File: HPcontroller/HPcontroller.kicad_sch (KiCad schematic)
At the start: 8 parts, among them J5 54-00174, U7 Adafruit_QTPY_ESP32-C3

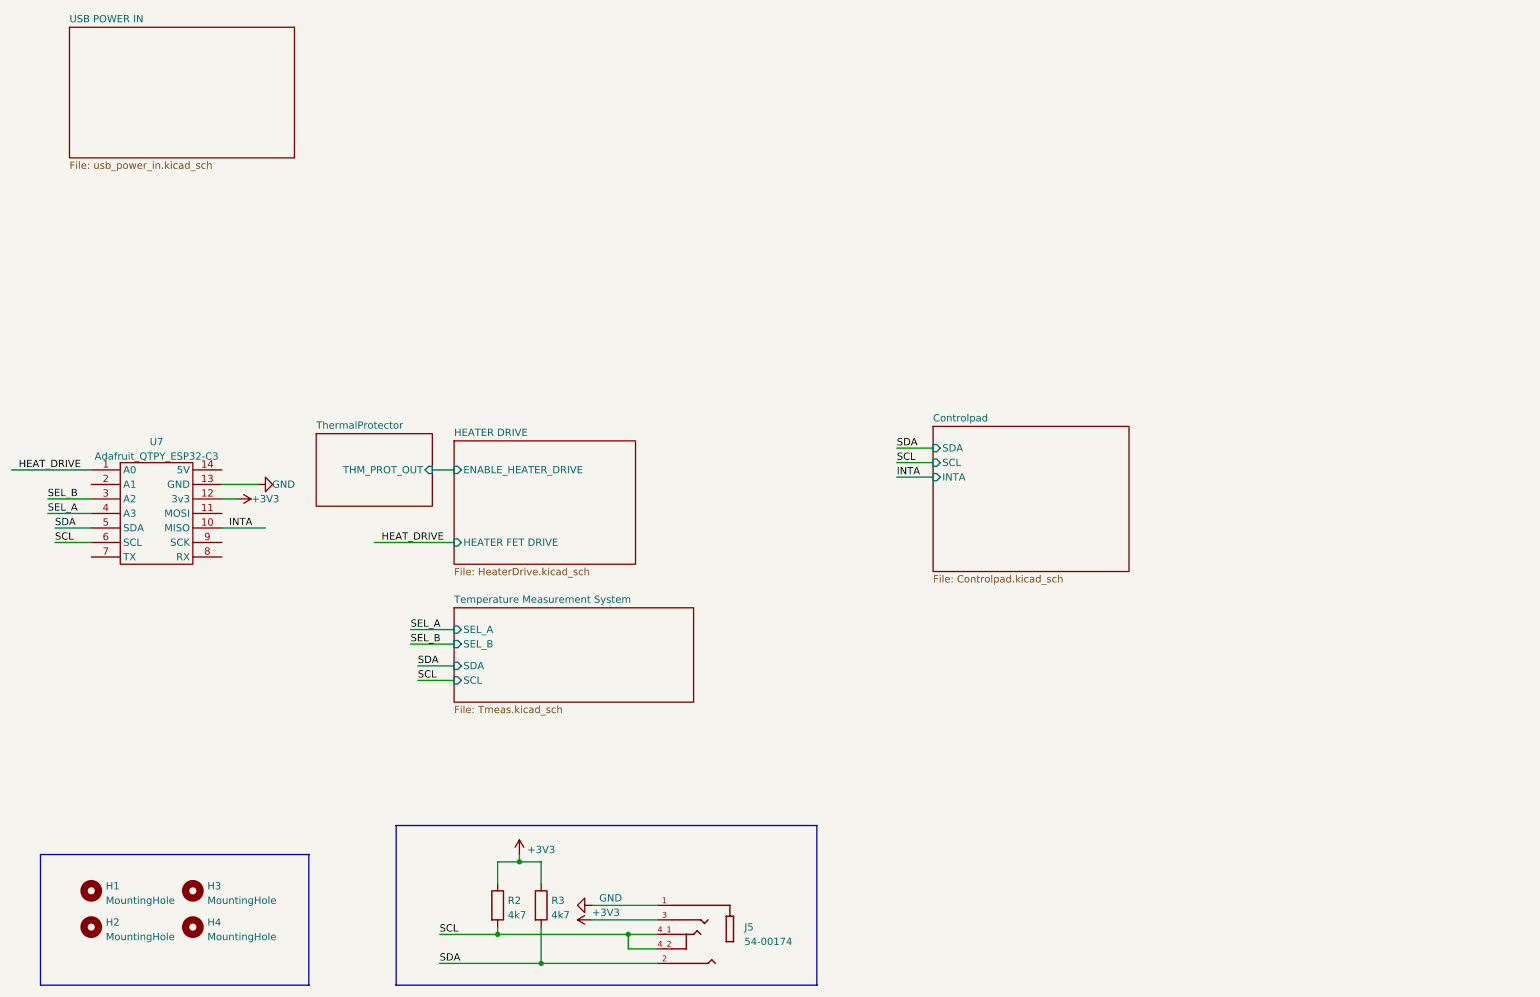
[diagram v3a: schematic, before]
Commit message: worked on bom, orderables from dk are in
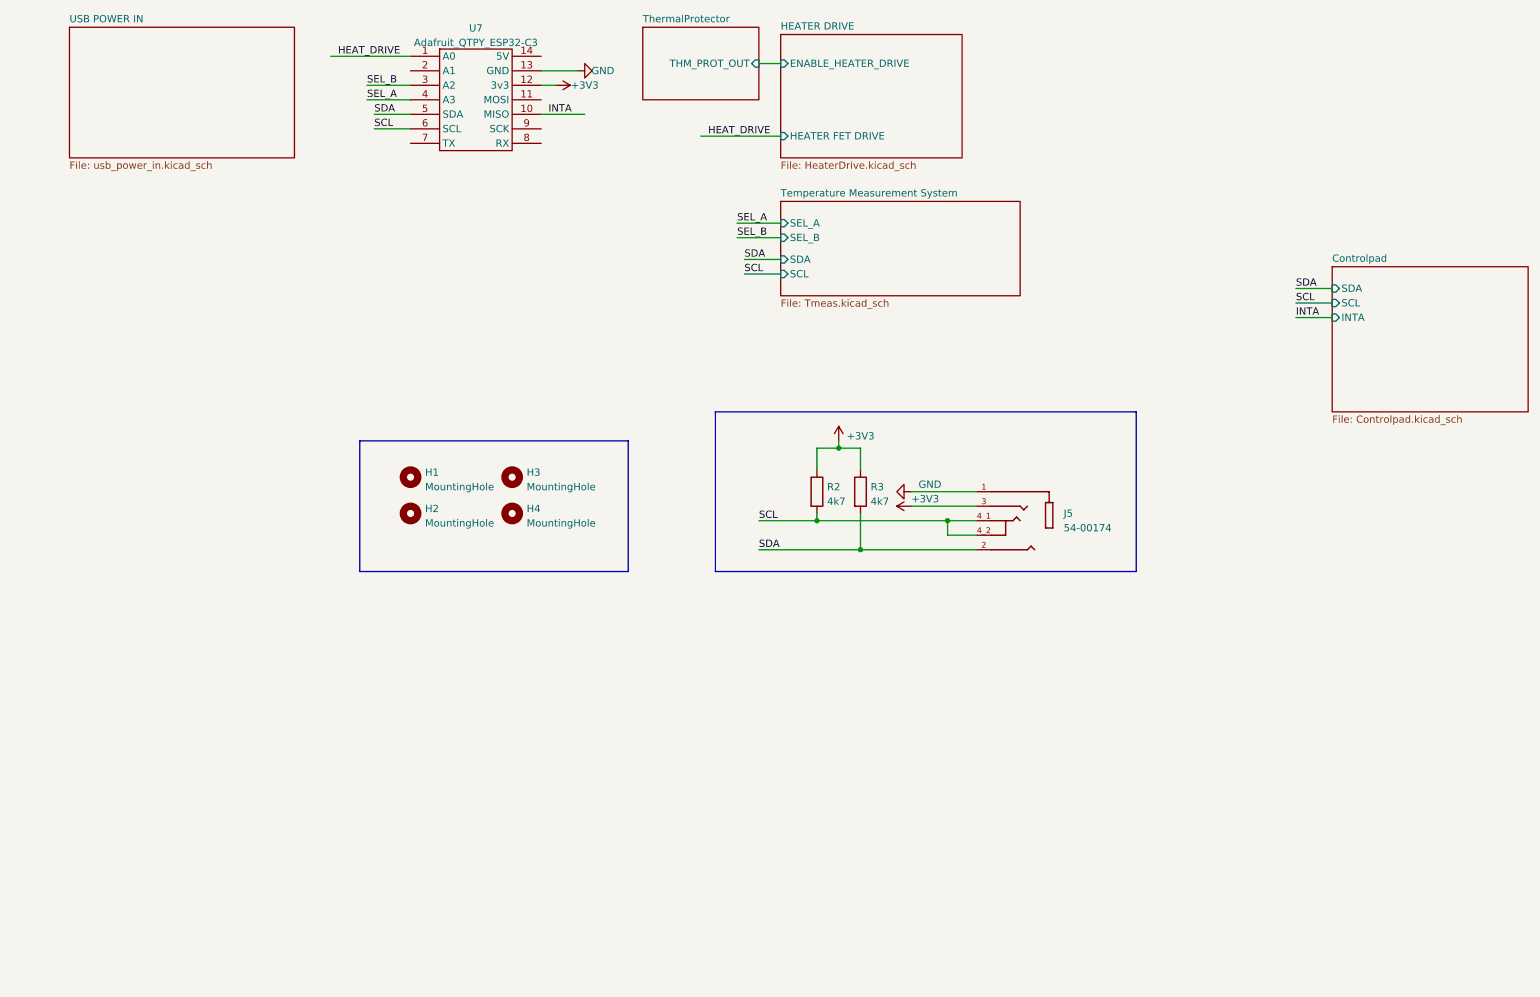
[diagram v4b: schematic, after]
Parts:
- J5: Digikey PN (none) -> 839-54-00174CT-ND; SNAPEDA_PN 54-00174 -> (none)
- R2, R3: Digikey PN (none) -> 311-4.7KARCT-ND; MPN (none) -> RC0805JR-074K7L
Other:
- moved on the sheet: H1, H2, H3, H4, J5, R2, R3, U7

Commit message: v3 routing
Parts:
- U7: footprint HPfootprint:QTPY ESP32 C3 -> hotplate_Library:XIAO-ESP32C3-SMD-cutout
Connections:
- net INTA: no longer names the net of U7.10 (MISO)
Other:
- removed sheet Controlpad

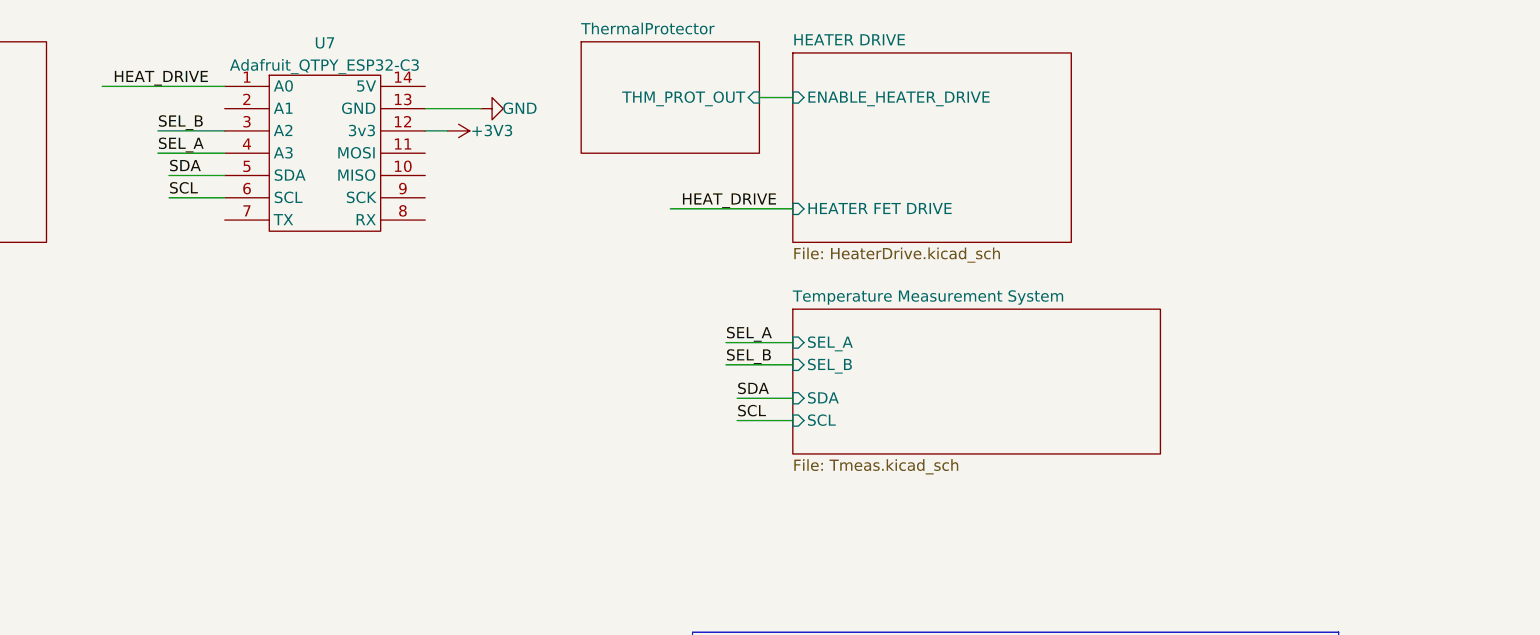
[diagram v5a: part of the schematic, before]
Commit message: new temp circuit
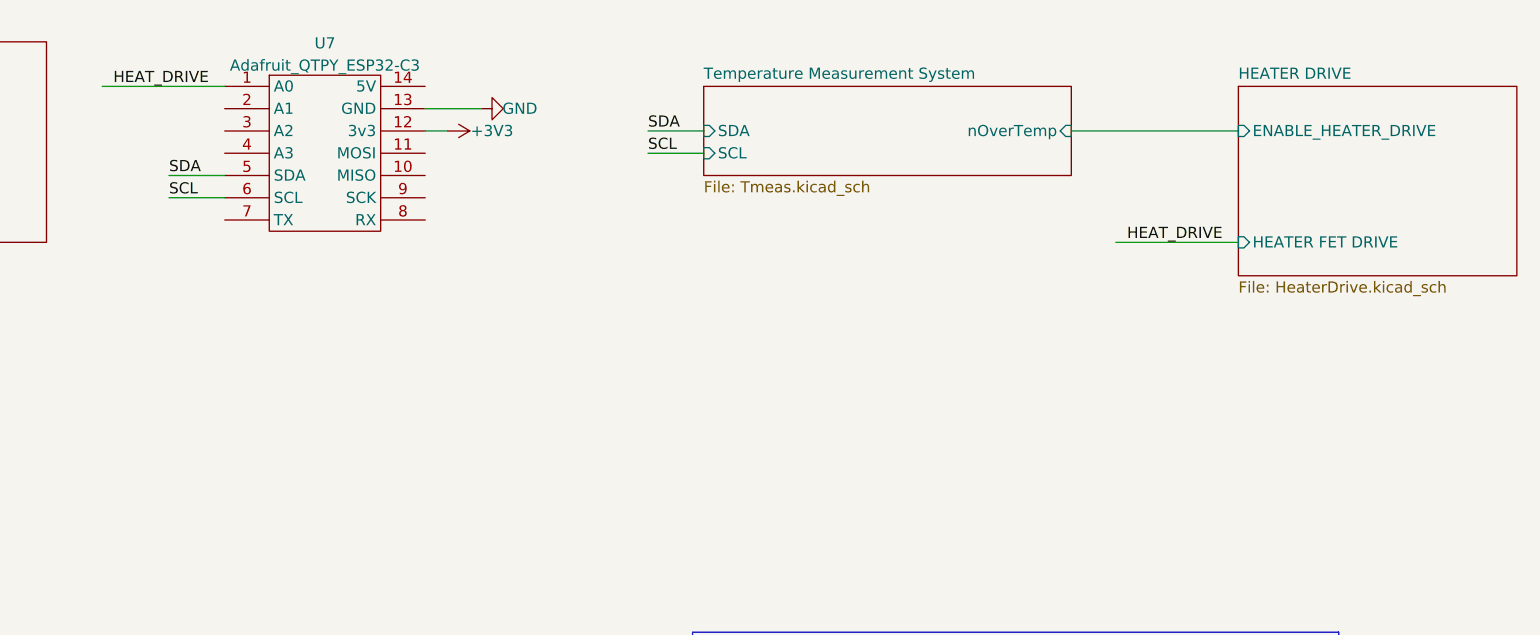
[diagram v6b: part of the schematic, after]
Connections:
- net SEL_A: no longer names the net of U7.4 (A3)
- net SEL_B: no longer names the net of U7.3 (A2)
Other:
- removed sheet ThermalProtector
- sheet Temperature Measurement System ports: added nOverTemp; removed SEL_A, SEL_B
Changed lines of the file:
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@@
 	(wire
 		(pts
-			(xy 144.78 66.04) (xy 151.13 66.04)
+			(xy 134.62 35.56) (xy 140.97 35.56)
 		)
 		(stroke
@@
 	(wire
 		(pts
-			(xy 78.74 35.56) (xy 86.36 35.56)
-		)
-		(stroke
-			(width 0)
-			(type default)
-		)
-	)
-	(wire
-		(pts
-			(xy 143.51 62.23) (xy 151.13 62.23)
-		)
-		(stroke
-			(width 0)
-			(type default)
-		)
-	)
-	(wire
-		(pts
 			(xy 180.34 114.3) (xy 180.34 111.76)
 		)
@@
 	(wire
 		(pts
-			(xy 144.78 68.58) (xy 151.13 68.58)
+			(xy 134.62 38.1) (xy 140.97 38.1)
 		)
 		(stroke
@@
 	(wire
 		(pts
+			(xy 182.88 35.56) (xy 201.93 35.56)
+		)
+		(stroke
+			(width 0)
+			(type default)
+		)
+	)
+	(wire
+		(pts
 			(xy 161.29 99.06) (xy 165.1 99.06)
 		)
@@
 	(wire
 		(pts
-			(xy 147.32 31.75) (xy 151.13 31.75)
-		)
-		(stroke
-			(width 0)
-			(type default)
-		)
-	)
-	(wire
-		(pts
 			(xy 165.1 116.84) (xy 185.42 116.84)
 		)
@@
 	(wire
 		(pts
-			(xy 137.16 44.45) (xy 151.13 44.45)
+			(xy 187.96 48.26) (xy 201.93 48.26)
 		)
 		(stroke
@@
 		)
 	)
-	(wire
-		(pts
-			(xy 78.74 38.1) (xy 86.36 38.1)
-		)
-		(stroke
-			(width 0)
-			(type default)
-		)
-	)
 	(polyline
 		(pts
@@
 	(wire
 		(pts
-			(xy 143.51 59.69) (xy 151.13 59.69)
-		)
-		(stroke
-			(width 0)
-			(type default)
-		)
-	)
-	(wire
-		(pts
 			(xy 173.99 109.22) (xy 185.42 109.22)
 		)
@@
 		)
 	)
-	(label "SEL_B"
-		(at 78.74 35.56 0)
-		(effects
-			(font
-				(size 1.27 1.27)
-			)
-			(justify left bottom)
-		)
-	)
 	(label "SDA"
-		(at 144.78 66.04 0)
+		(at 134.62 35.56 0)
 		(effects
 			(font
@@
 		)
 	)
-	(label "SEL_B"
-		(at 143.51 62.23 0)
-		(effects
-			(font
-				(size 1.27 1.27)
-			)
-			(justify left bottom)
-		)
-	)
 	(label "SCL"
-		(at 144.78 68.58 0)
-		(effects
-			(font
-				(size 1.27 1.27)
-			)
-			(justify left bottom)
-		)
-	)
-	(label "SEL_A"
-		(at 78.74 38.1 0)
-		(effects
-			(font
-				(size 1.27 1.27)
-			)
-			(justify left bottom)
-		)
-	)
-	(label "SEL_A"
-		(at 143.51 59.69 0)
+		(at 134.62 38.1 0)
 		(effects
 			(font
@@
 	)
 	(label "HEAT_DRIVE"
-		(at 138.43 44.45 0)
+		(at 189.23 48.26 0)
 		(effects
 			(font
@@
 	)
 	(sheet
-		(at 151.13 55.88)
-		(size 41.91 16.51)
+		(at 140.97 30.48)
+		(size 41.91 10.16)
 		(exclude_from_sim no)
 		(in_bom yes)
@@
 		)
 		(property "Sheetname" "Temperature Measurement System"
-			(at 151.13 55.1684 0)
+			(at 140.97 29.7684 0)
 			(effects
 				(font
@@
 		)
 		(property "Sheetfile" "Tmeas.kicad_sch"
-			(at 151.13 72.9746 0)
+			(at 140.97 41.2246 0)
 			(effects
 				(font
@@
 			)
 		)
-		(pin "SEL_B" input
-			(at 151.13 62.23 180)
-			(effects
-				(font
-					(size 1.27 1.27)
-				)
-				(justify left)
-			)
-		)
 		(pin "SDA" input
-			(at 151.13 66.04 180)
+			(at 140.97 35.56 180)
 			(effects
 				(font
@@
 		)
 		(pin "SCL" input
-			(at 151.13 68.58 180)
-			(effects
-				(font
-					(size 1.27 1.27)
-				)
-				(justify left)
-			)
-		)
-		(pin "SEL_A" input
-			(at 151.13 59.69 180)
-			(effects
-				(font
-					(size 1.27 1.27)
-				)
-				(justify left)
+			(at 140.97 38.1 180)
+			(effects
+				(font
+					(size 1.27 1.27)
+				)
+				(justify left)
+			)
+		)
+		(pin "nOverTemp" input
+			(at 182.88 35.56 0)
+			(effects
+				(font
+					(size 1.27 1.27)
+				)
+				(justify right)
 			)
 		)
@@
 	)
 	(sheet
-		(at 127 25.4)
-		(size 20.32 12.7)
-		(exclude_from_sim no)
-		(in_bom yes)
-		(on_board yes)
-		(dnp no)
-		(stroke
-			(width 0.1524)
-			(type solid)
-		)
-		(fill
-			(color 0 0 0 0.0000)
-		)
-		(property "Sheetname" "ThermalProtector"
-			(at 127 24.6884 0)
-			(effects
-				(font
-					(size 1.27 1.27)
-				)
-				(justify left bottom)
-			)
-		)
-		(property "Sheetfile" "ThermalProtector.kicad_sch"
-			(at 115.57 39.37 0)
-			(effects
-				(font
-					(size 1.27 1.27)
-				)
-				(justify left top)
-				(hide yes)
-			)
-		)
-		(pin "THM_PROT_OUT" input
-			(at 147.32 31.75 0)
-			(effects
-				(font
-					(size 1.27 1.27)
-				)
-				(justify right)
-			)
-		)
-		(instances
-			(project "HPcontroller"
-				(path "/e63e39d7-6ac0-4ffd-8aa3-1841a4541b55"
-					(page "2")
-				)
-			)
-		)
-	)
-	(sheet
-		(at 151.13 26.67)
+		(at 201.93 30.48)
 		(size 31.75 21.59)
 		(exclude_from_sim no)
@@
 		)
 		(property "Sheetname" "HEATER DRIVE"
-			(at 151.13 25.9584 0)
+			(at 201.93 29.7684 0)
 			(effects
 				(font
@@
 		)
 		(property "Sheetfile" "HeaterDrive.kicad_sch"
-			(at 151.13 48.8446 0)
+			(at 201.93 52.6546 0)
 			(effects
 				(font
@@
 		)
 		(pin "ENABLE_HEATER_DRIVE" input
-			(at 151.13 31.75 180)
+			(at 201.93 35.56 180)
 			(effects
 				(font
@@
 		)
 		(pin "HEATER FET DRIVE" input
-			(at 151.13 44.45 180)
-			(effects
-				(font
+			(at 201.93 48.26 180)
+			(effects
+				(font
